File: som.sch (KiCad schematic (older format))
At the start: 21 parts, among them M1 SC606T

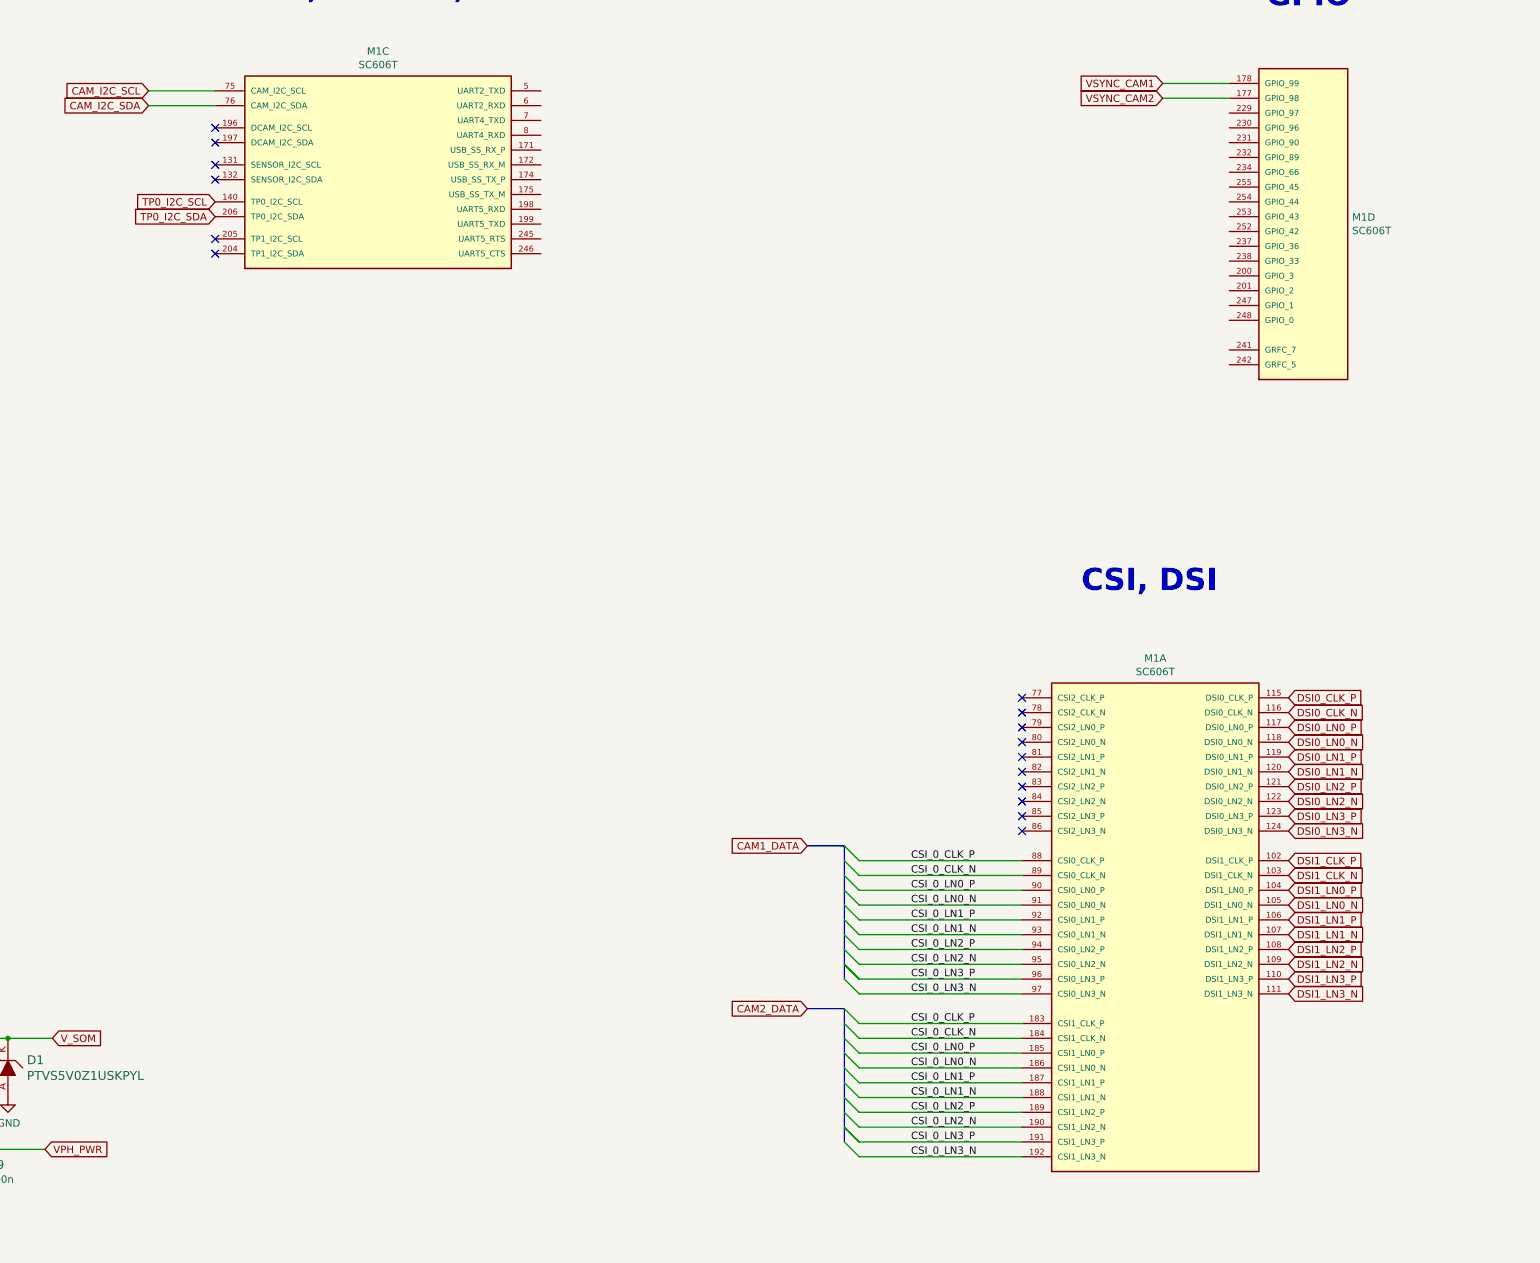
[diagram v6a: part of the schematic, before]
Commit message: Finished connection to HDMI interface. Adjustments after Update of LT9611 symbol
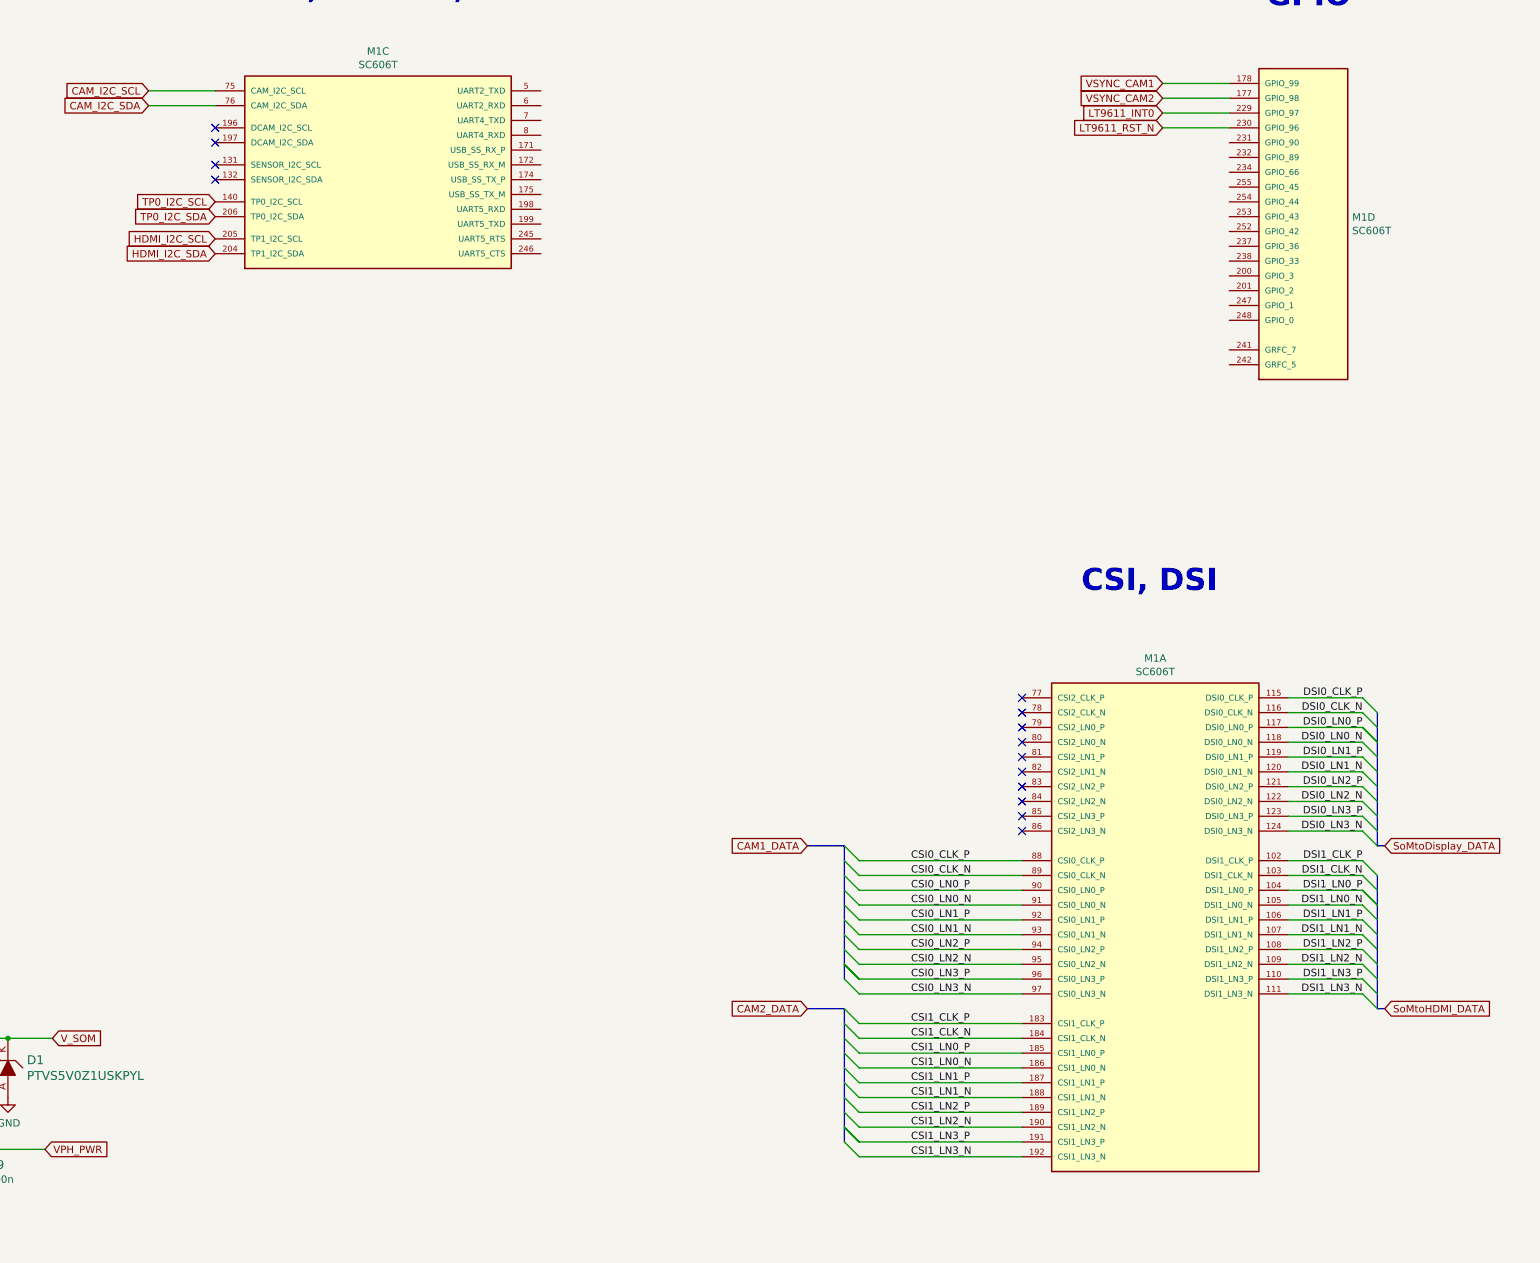
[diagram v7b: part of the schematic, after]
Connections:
- net HDMI_I2C_SDA: now reaches M1.204 (TP1_I2C_SDA)
- net HDMI_I2C_SCL: now reaches M1.205 (TP1_I2C_SCL)
- net LT9611_INT0: now reaches M1.229 (GPIO_97)
- net LT9611_RST_N: now reaches M1.230 (GPIO_96)
- net CSI_0_CLK_N renamed CSI0_CLK_N
- net CSI0_CLK_N: no longer M1.184 (CSI1_CLK_N)
- net CSI_0_CLK_P renamed CSI0_CLK_P
- net CSI0_CLK_P: no longer M1.183 (CSI1_CLK_P)
- net CSI_0_LN0_N renamed CSI0_LN0_N
- net CSI0_LN0_N: no longer M1.186 (CSI1_LN0_N)
- net CSI_0_LN0_P renamed CSI0_LN0_P
- net CSI0_LN0_P: no longer M1.185 (CSI1_LN0_P)
- net CSI_0_LN1_N renamed CSI0_LN1_N
- net CSI0_LN1_N: no longer M1.188 (CSI1_LN1_N)
- net CSI_0_LN1_P renamed CSI0_LN1_P
- net CSI0_LN1_P: no longer M1.187 (CSI1_LN1_P)
- net CSI_0_LN2_N renamed CSI0_LN2_N
- net CSI0_LN2_N: no longer M1.190 (CSI1_LN2_N)
- net CSI_0_LN2_P renamed CSI0_LN2_P
- net CSI0_LN2_P: no longer M1.189 (CSI1_LN2_P)
- net CSI_0_LN3_N renamed CSI0_LN3_N
- net CSI0_LN3_N: no longer M1.192 (CSI1_LN3_N)
- net CSI_0_LN3_P renamed CSI0_LN3_P
- net CSI0_LN3_P: no longer M1.191 (CSI1_LN3_P)
- new net CSI1_CLK_N: M1.184 (CSI1_CLK_N)
- new net CSI1_CLK_P: M1.183 (CSI1_CLK_P)
- new net CSI1_LN0_N: M1.186 (CSI1_LN0_N)
- new net CSI1_LN0_P: M1.185 (CSI1_LN0_P)
- new net CSI1_LN1_N: M1.188 (CSI1_LN1_N)
- new net CSI1_LN1_P: M1.187 (CSI1_LN1_P)
- new net CSI1_LN2_N: M1.190 (CSI1_LN2_N)
- new net CSI1_LN2_P: M1.189 (CSI1_LN2_P)
- new net CSI1_LN3_N: M1.192 (CSI1_LN3_N)
- new net CSI1_LN3_P: M1.191 (CSI1_LN3_P)
- no-connect marks 88 -> 86
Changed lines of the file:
@@
 	12850 7700 11750 7700
 Text Label 12100 7100 0    50   ~ 0
-CSI_0_LN0_N
+CSI0_LN0_N
 Text Label 12100 7000 0    50   ~ 0
-CSI_0_LN0_P
+CSI0_LN0_P
 Text Label 12100 7300 0    50   ~ 0
-CSI_0_LN1_N
+CSI0_LN1_N
 Text Label 12100 7200 0    50   ~ 0
-CSI_0_LN1_P
+CSI0_LN1_P
 Text Label 12100 7500 0    50   ~ 0
-CSI_0_LN2_N
+CSI0_LN2_N
 Text Label 12100 7400 0    50   ~ 0
-CSI_0_LN2_P
+CSI0_LN2_P
 Text Label 12100 7700 0    50   ~ 0
-CSI_0_LN3_N
+CSI0_LN3_N
 Text Label 12100 7600 0    50   ~ 0
-CSI_0_LN3_P
+CSI0_LN3_P
 Text Label 12100 6900 0    50   ~ 0
-CSI_0_CLK_N
+CSI0_CLK_N
 Text Label 12100 6800 0    50   ~ 0
-CSI_0_CLK_P
+CSI0_CLK_P
 Text GLabel 11400 6700 0    50   Input ~ 0
 CAM1_DATA
@@
 Entry Wire Line
 	11650 7900 11750 8000
-Wire Wire Line
-	12850 8200 11750 8200
-Wire Wire Line
-	11750 8300 12850 8300
-Wire Wire Line
-	12850 8400 11750 8400
-Wire Wire Line
-	11750 8500 12850 8500
-Wire Wire Line
-	12850 8600 11750 8600
-Wire Wire Line
-	11750 8700 12850 8700
-Wire Wire Line
-	12850 8800 11750 8800
-Text Label 12100 8200 0    50   ~ 0
-CSI_0_LN0_N
-Text Label 12100 8100 0    50   ~ 0
-CSI_0_LN0_P
-Text Label 12100 8400 0    50   ~ 0
-CSI_0_LN1_N
-Text Label 12100 8300 0    50   ~ 0
-CSI_0_LN1_P
-Text Label 12100 8600 0    50   ~ 0
-CSI_0_LN2_N
-Text Label 12100 8500 0    50   ~ 0
-CSI_0_LN2_P
-Text Label 12100 8800 0    50   ~ 0
-CSI_0_LN3_N
-Text Label 12100 8700 0    50   ~ 0
-CSI_0_LN3_P
-Text Label 12100 8000 0    50   ~ 0
-CSI_0_CLK_N
-Text Label 12100 7900 0    50   ~ 0
-CSI_0_CLK_P
 Text GLabel 11400 7800 0    50   Input ~ 0
 CAM2_DATA
 Wire Bus Line
 	11650 7800 11400 7800
-Wire Wire Line
-	11750 8100 12850 8100
 Entry Wire Line
 	11650 8600 11750 8700
 Entry Wire Line
 	11650 8600 11750 8700
-Wire Wire Line
-	11750 7900 12850 7900
-Wire Wire Line
-	11750 8000 12850 8000
 Entry Wire Line
 	11650 8700 11750 8800
@@
 NoConn ~ 5000 2450
 NoConn ~ 5000 2550
-NoConn ~ 7400 2600
-NoConn ~ 7400 2700
 NoConn ~ 5000 2150
 NoConn ~ 5000 2050
@@
 NoConn ~ 5000 5750
 NoConn ~ 5000 5850
-Text GLabel 14650 7700 2    50   Input ~ 0
+Text Label 15150 7700 2    50   ~ 0
 DSI1_LN3_N
-Text GLabel 14650 7600 2    50   Input ~ 0
+Text Label 15150 7600 2    50   ~ 0
 DSI1_LN3_P
-Text GLabel 14650 7500 2    50   Input ~ 0
+Text Label 15150 7500 2    50   ~ 0
 DSI1_LN2_N
-Text GLabel 14650 7400 2    50   Input ~ 0
+Text Label 15150 7400 2    50   ~ 0
 DSI1_LN2_P
-Text GLabel 14650 7300 2    50   Input ~ 0
+Text Label 15150 6900 2    50   ~ 0
+DSI1_CLK_N
+Text Label 15150 6800 2    50   ~ 0
+DSI1_CLK_P
+Text Label 15150 7300 2    50   ~ 0
 DSI1_LN1_N
-Text GLabel 14650 7200 2    50   Input ~ 0
+Text Label 15150 7200 2    50   ~ 0
 DSI1_LN1_P
-Text GLabel 14650 7100 2    50   Input ~ 0
+Text Label 15150 7100 2    50   ~ 0
 DSI1_LN0_N
-Text GLabel 14650 7000 2    50   Input ~ 0
+Text Label 15150 7000 2    50   ~ 0
 DSI1_LN0_P
-Text GLabel 14650 6900 2    50   Input ~ 0
-DSI1_CLK_N
-Text GLabel 14650 6800 2    50   Input ~ 0
-DSI1_CLK_P
-Text GLabel 14650 6600 2    50   Input ~ 0
+Wire Wire Line
+	14650 7700 15150 7700
+Wire Wire Line
+	15150 7600 14650 7600
+Wire Wire Line
+	14650 7500 15150 7500
+Wire Wire Line
+	15150 7400 14650 7400
+Wire Wire Line
+	14650 6900 15150 6900
+Wire Wire Line
+	15150 6800 14650 6800
+Wire Wire Line
+	14650 7300 15150 7300
+Wire Wire Line
+	15150 7200 14650 7200
+Wire Wire Line
+	14650 7100 15150 7100
+Wire Wire Line
+	15150 7000 14650 7000
+Entry Wire Line
+	15250 7800 15150 7700
+Entry Wire Line
+	15250 7700 15150 7600
+Entry Wire Line
+	15250 7600 15150 7500
+Entry Wire Line
+	15250 7500 15150 7400
+Entry Wire Line
+	15250 7400 15150 7300
+Entry Wire Line
+	15250 7300 15150 7200
+Entry Wire Line
+	15250 7200 15150 7100
+Entry Wire Line
+	15250 7100 15150 7000
+Entry Wire Line
+	15250 7100 15150 7000
+Entry Wire Line
+	15250 7000 15150 6900
+Entry Wire Line
+	15250 6900 15150 6800
+Wire Bus Line
+	15250 7800 15300 7800
+Text GLabel 15300 7800 2    50   Input ~ 0
+SoMtoHDMI_DATA
+Text Label 15150 6600 2    50   ~ 0
 DSI0_LN3_N
-Text GLabel 14650 6500 2    50   Input ~ 0
+Text Label 15150 6500 2    50   ~ 0
 DSI0_LN3_P
-Text GLabel 14650 6400 2    50   Input ~ 0
+Text Label 15150 6400 2    50   ~ 0
 DSI0_LN2_N
-Text GLabel 14650 6300 2    50   Input ~ 0
+Text Label 15150 6300 2    50   ~ 0
 DSI0_LN2_P
-Text GLabel 14650 6200 2    50   Input ~ 0
+Text Label 15150 5800 2    50   ~ 0
+DSI0_CLK_N
+Text Label 15150 5700 2    50   ~ 0
+DSI0_CLK_P
+Text Label 15150 6200 2    50   ~ 0
 DSI0_LN1_N
-Text GLabel 14650 6100 2    50   Input ~ 0
+Text Label 15150 6100 2    50   ~ 0
 DSI0_LN1_P
-Text GLabel 14650 6000 2    50   Input ~ 0
+Text Label 15150 6000 2    50   ~ 0
 DSI0_LN0_N
+Text Label 15150 5900 2    50   ~ 0
+DSI0_LN0_P
+Wire Wire Line
+	14650 6600 15150 6600
+Wire Wire Line
+	15150 6500 14650 6500
+Wire Wire Line
+	14650 6400 15150 6400
+Wire Wire Line
+	15150 6300 14650 6300
+Wire Wire Line
+	14650 5800 15150 5800
+Wire Wire Line
+	15150 5700 14650 5700
+Wire Wire Line
+	14650 6200 15150 6200
+Wire Wire Line
+	15150 6100 14650 6100
+Wire Wire Line
+	14650 6000 15150 6000
+Wire Wire Line
+	15150 5900 14650 5900
+Entry Wire Line
+	15250 6700 15150 6600
+Entry Wire Line
+	15250 6600 15150 6500
+Entry Wire Line
+	15250 6500 15150 6400
+Entry Wire Line
+	15250 6400 15150 6300
+Entry Wire Line
+	15250 6300 15150 6200
+Entry Wire Line
+	15250 6200 15150 6100
+Entry Wire Line
+	15250 6100 15150 6000
+Entry Wire Line
+	15250 6000 15150 5900
+Entry Wire Line
+	15250 6000 15150 5900
+Entry Wire Line
+	15250 5900 15150 5800
+Entry Wire Line
+	15250 5800 15150 5700
+Wire Bus Line
+	15250 6700 15300 6700
+Text GLabel 15300 6700 2    50   Input ~ 0
+SoMtoDisplay_DATA
+Text GLabel 7400 2600 0    50   Input ~ 0
+HDMI_I2C_SCL
+Text GLabel 7400 2700 0    50   Input ~ 0
+HDMI_I2C_SDA
+Text Label 12100 8200 0    50   ~ 0
+CSI1_LN0_N
+Text Label 12100 8100 0    50   ~ 0
+CSI1_LN0_P
+Text Label 12100 8400 0    50   ~ 0
+CSI1_LN1_N
+Text Label 12100 8300 0    50   ~ 0
+CSI1_LN1_P
+Text Label 12100 8600 0    50   ~ 0
+CSI1_LN2_N
+Text Label 12100 8500 0    50   ~ 0
+CSI1_LN2_P
+Text Label 12100 8800 0    50   ~ 0
+CSI1_LN3_N
+Text Label 12100 8700 0    50   ~ 0
+CSI1_LN3_P
+Text Label 12100 8000 0    50   ~ 0
+CSI1_CLK_N
+Text Label 12100 7900 0    50   ~ 0
+CSI1_CLK_P
+Wire Wire Line
+	11750 8100 12850 8100
+Wire Wire Line
+	12850 8200 11750 8200
+Wire Wire Line
+	11750 8300 12850 8300
+Wire Wire Line
+	12850 8400 11750 8400
+Wire Wire Line
+	11750 8500 12850 8500
+Wire Wire Line
+	12850 8600 11750 8600
+Wire Wire Line
+	11750 8700 12850 8700
+Wire Wire Line
+	12850 8800 11750 8800
+Wire Wire Line
+	11750 7900 12850 7900
+Wire Wire Line
+	11750 8000 12850 8000
+Text GLabel 13800 1750 0    50   Input ~ 0
+LT9611_INT0
+Text GLabel 13800 1850 0    50   Input ~ 0
+LT9611_RST_N
+Wire Wire Line
+	13800 1750 14250 1750
+Wire Wire Line
+	14250 1850 13800 1850
 Wire Bus Line
 	1750 4650 1750 5350
@@
 Wire Bus Line
 	11650 7800 11650 8700
-Text GLabel 14650 5900 2    50   Input ~ 0
-DSI0_LN0_P
-Text GLabel 14650 5800 2    50   Input ~ 0
-DSI0_CLK_N
-Text GLabel 14650 5700 2    50   Input ~ 0
-DSI0_CLK_P
+Wire Bus Line
+	15250 6900 15250 7800
+Wire Bus Line
+	15250 5800 15250 6700
 $EndSCHEMATC

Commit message: Modifications after P. Szczygiel review
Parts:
- removed C15: C_33p_0402, sc606-baseboard-footprints:0402-cap, symbol sc606-baseboard:C_33p_0402
- added C?: C_1u_0402, antmicro-footprints:0402-cap, symbol antmicroCapacitors0402:C_1u_0402
- added R? (x2): R_2k_0402, sc606-baseboard-footprints:0402-res, symbol sc606-baseboard:R_2k_0402
- added TP? (x10): TestPoint, symbol Connector:TestPoint
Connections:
- net GND: now also C?.2
- net LDO6_1P8: now also C?.1, R?.1, R?.1
- net at M1.131 (SENSOR_I2C_SCL): now also R?.2, TP?.1
- net at M1.132 (SENSOR_I2C_SDA): now also R?.2, TP?.1
- net at M1.5 (UART2_TXD): now also TP?.1
- net at M1.6 (UART2_RXD): now also TP?.1
- net at M1.200 (GPIO_3): now also TP?.1
- net at M1.201 (GPIO_2): now also TP?.1
- net at M1.237 (GPIO_36): now also TP?.1
- net at M1.238 (GPIO_33): now also TP?.1
- net at M1.247 (GPIO_1): now also TP?.1
- net at M1.248 (GPIO_0): now also TP?.1
- no-connect marks 86 -> 84
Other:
- moved on the sheet: M1A, M1D
